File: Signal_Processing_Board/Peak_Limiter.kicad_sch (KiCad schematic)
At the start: 21 parts, among them Q1 2N3819, U5 TL084

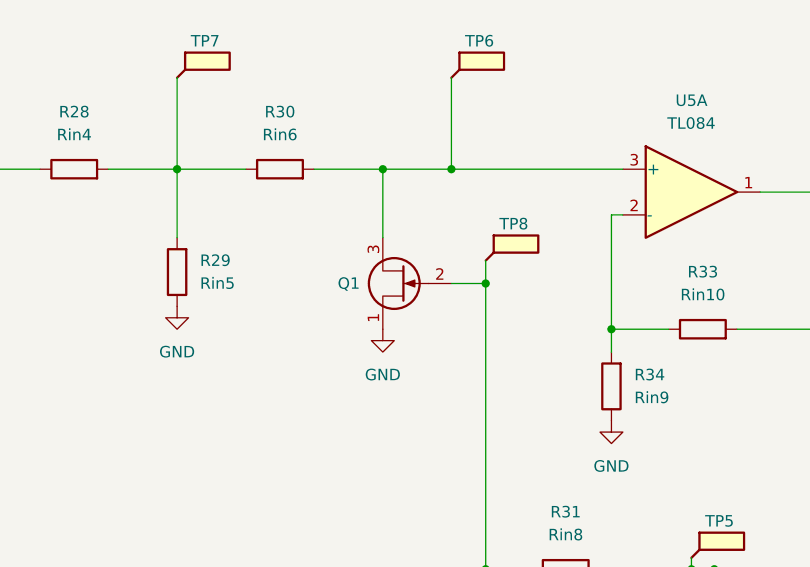
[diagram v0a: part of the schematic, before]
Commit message: Final version of the board, updated with lessons from first version
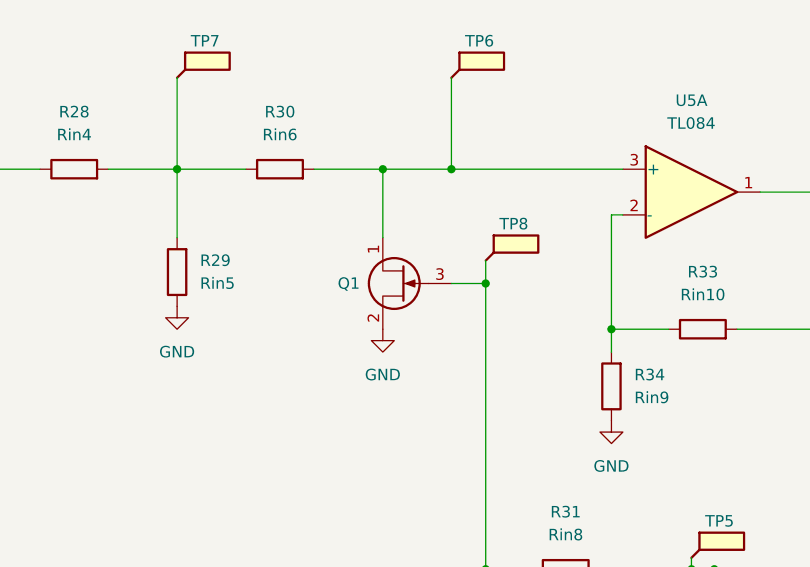
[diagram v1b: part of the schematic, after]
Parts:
- Q1: footprint Package_TO_SOT_THT:TO-92 -> Package_TO_SOT_THT:TO-92_Inline
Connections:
- net GND: now also Q1.2 (D); no longer Q1.1 (D)
- net at R31.1, R32.2, TP8.1: now also Q1.3 (G); no longer Q1.2 (G)
- net at R30.2, TP6.1, U5.3 (+): now also Q1.1 (S); no longer Q1.3 (S)
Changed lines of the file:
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@@
 			)
 		)
-		(property "Footprint" "Package_TO_SOT_THT:TO-92"
+		(property "Footprint" "Package_TO_SOT_THT:TO-92_Inline"
 			(at 102.87 74.295 0)
 			(effects

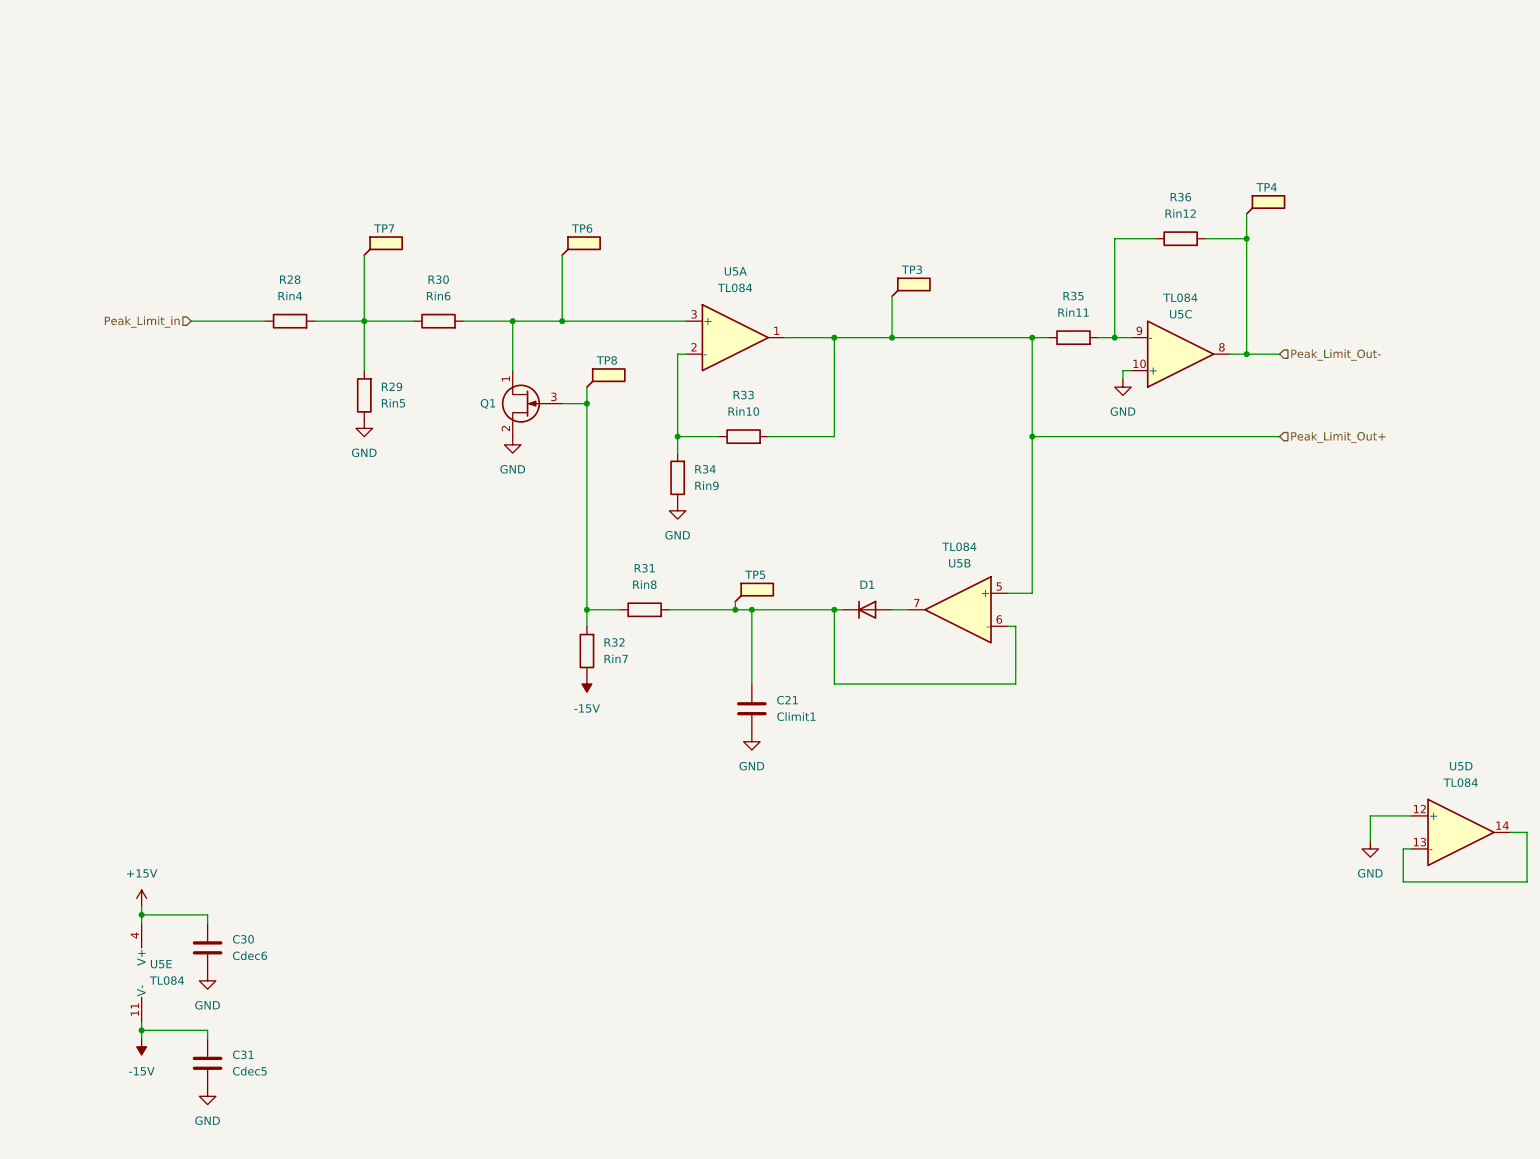
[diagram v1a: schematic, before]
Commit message: Updated file structure and added PDF of schematic
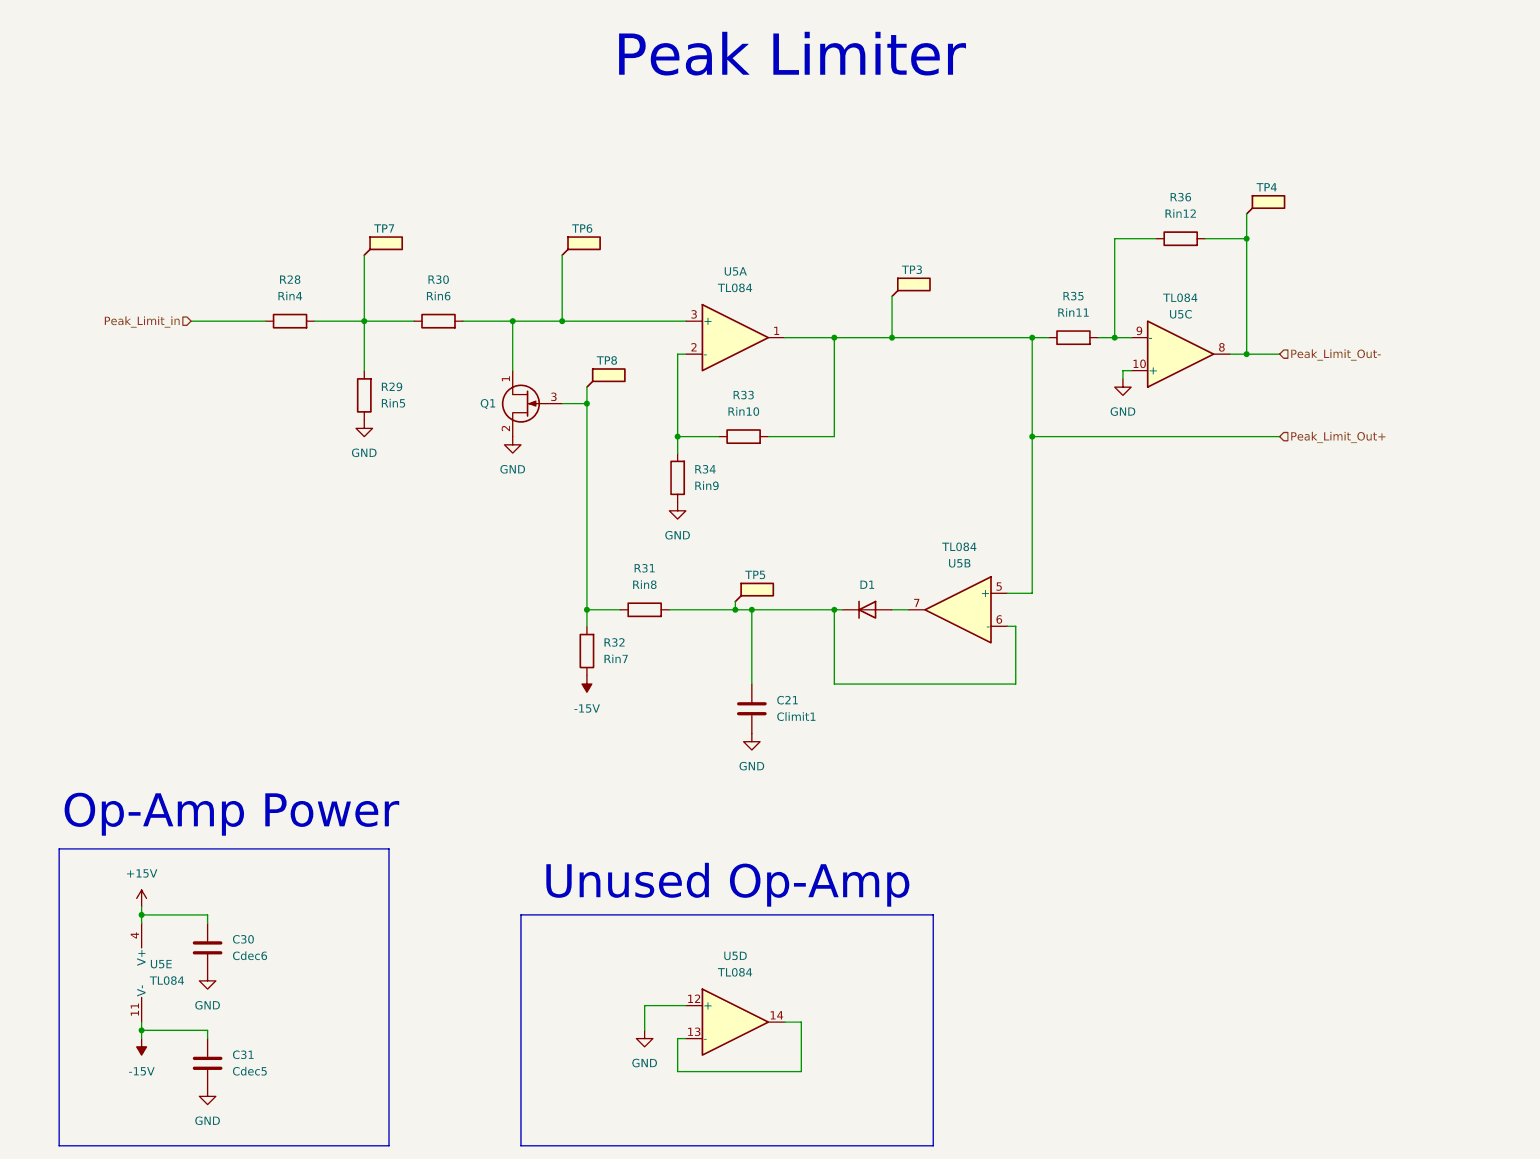
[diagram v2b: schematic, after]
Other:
- note added: "Op-Amp Power"
- note added: "Peak Limiter"
- note added: "Unused Op-Amp"
- moved on the sheet: U5D
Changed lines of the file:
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@@
 	(wire
 		(pts
-			(xy 243.84 144.78) (xy 242.57 144.78)
+			(xy 132.08 173.99) (xy 130.81 173.99)
 		)
 		(stroke
@@
 	(wire
 		(pts
-			(xy 242.57 144.78) (xy 242.57 149.86)
+			(xy 130.81 173.99) (xy 130.81 179.07)
 		)
 		(stroke
@@
 	(wire
 		(pts
-			(xy 243.84 139.7) (xy 237.49 139.7)
-		)
-		(stroke
-			(width 0)
-			(type default)
-		)
-	)
-	(wire
-		(pts
-			(xy 237.49 139.7) (xy 237.49 143.51)
+			(xy 132.08 168.91) (xy 125.73 168.91)
+		)
+		(stroke
+			(width 0)
+			(type default)
+		)
+	)
+	(wire
+		(pts
+			(xy 125.73 168.91) (xy 125.73 172.72)
 		)
 		(stroke
@@
 	(wire
 		(pts
-			(xy 242.57 149.86) (xy 261.62 149.86)
+			(xy 130.81 179.07) (xy 149.86 179.07)
 		)
 		(stroke
@@
 	(wire
 		(pts
-			(xy 261.62 142.24) (xy 259.08 142.24)
+			(xy 149.86 171.45) (xy 147.32 171.45)
 		)
 		(stroke
@@
 	(wire
 		(pts
-			(xy 261.62 149.86) (xy 261.62 142.24)
+			(xy 149.86 179.07) (xy 149.86 171.45)
 		)
 		(stroke
@@
 			(width 0)
 			(type default)
+		)
+	)
+	(rectangle
+		(start 35.56 144.78)
+		(end 86.36 190.5)
+		(stroke
+			(width 0)
+			(type default)
+		)
+		(fill
+			(type none)
+		)
+	)
+	(rectangle
+		(start 106.68 154.94)
+		(end 170.18 190.5)
+		(stroke
+			(width 0)
+			(type default)
+		)
+		(fill
+			(type none)
+		)
+	)
+	(text "Op-Amp Power"
+		(exclude_from_sim no)
+		(at 61.976 139.192 0)
+		(effects
+			(font
+				(size 5.08 5.08)
+			)
+		)
+	)
+	(text "Unused Op-Amp\n"
+		(exclude_from_sim no)
+		(at 138.43 150.114 0)
+		(effects
+			(font
+				(size 5.08 5.08)
+			)
+		)
+	)
+	(text "Peak Limiter"
+		(exclude_from_sim no)
+		(at 148.082 22.86 0)
+		(effects
+			(font
+				(size 6.35 6.35)
+			)
 		)
 	)
@@
 	(symbol
 		(lib_id "power:GND")
-		(at 237.49 143.51 0)
+		(at 125.73 172.72 0)
 		(unit 1)
 		(exclude_from_sim no)
@@
 		(fields_autoplaced yes)
 		(property "Reference" "#PWR060"
-			(at 237.49 149.86 0)
+			(at 125.73 179.07 0)
 			(effects
 				(font
@@
 		)
 		(property "Value" "GND"
-			(at 237.49 148.59 0)
+			(at 125.73 177.8 0)
 			(effects
 				(font
@@
 		)
 		(property "Footprint" ""
-			(at 237.49 143.51 0)
+			(at 125.73 172.72 0)
 			(effects
 				(font
@@
 		)
 		(property "Datasheet" ""
-			(at 237.49 143.51 0)
+			(at 125.73 172.72 0)
 			(effects
 				(font
@@
 		)
 		(property "Description" "Power symbol creates a global label with name \"GND\" , ground"
-			(at 237.49 143.51 0)
+			(at 125.73 172.72 0)
 			(effects
 				(font
@@
 	(symbol
 		(lib_id "Amplifier_Operational:TL084")
-		(at 251.46 142.24 0)
+		(at 139.7 171.45 0)
 		(unit 4)
 		(exclude_from_sim no)
@@
 		(fields_autoplaced yes)
 		(property "Reference" "U5"
-			(at 251.46 132.08 0)
+			(at 139.7 161.29 0)
 			(effects
 				(font
@@
 		)
 		(property "Value" "TL084"
-			(at 251.46 134.62 0)
+			(at 139.7 163.83 0)
 			(effects
 				(font
@@
 		)
 		(property "Footprint" "Package_DIP:CERDIP-14_W7.62mm_SideBrazed_LongPads_Socket"
-			(at 250.19 139.7 0)
+			(at 138.43 168.91 0)
 			(effects
 				(font
@@
 		)
 		(property "Datasheet" "http://www.ti.com/lit/ds/symlink/tl081.pdf"
-			(at 252.73 137.16 0)
+			(at 140.97 166.37 0)
 			(effects
 				(font
@@
 		)
 		(property "Description" "Quad JFET-Input Operational Amplifiers, DIP-14/SOIC-14/SSOP-14"
-			(at 251.46 142.24 0)
-			(effects
-				(font
+			(at 139.7 171.45 0)
+			(effects
+				(font
